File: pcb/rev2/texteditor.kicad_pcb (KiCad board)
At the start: 2 copper layers, 82 x 55 mm, 21 parts, among them J2 LCD IDC, J3 Power In (7v-20v), J4 LED, J5 Contrast Pot, J6 Brightness Pot, J7 SD_Card_Receptacle, Q1 BC547, SW1 Input Type Switch, SW2 Power Switch, U1 L7805

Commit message: switch towurth socket
need to reroute some stuff now
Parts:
- added C5: 100nF, Capacitor_THT:C_Disc_D4.7mm_W2.5mm_P5.00mm, F.Cu at (122.4, 143.6)
- added C6: 10uF, Capacitor_THT:C_Radial_D4.0mm_H5.0mm_P1.50mm, F.Cu at (136.2, 140.2)
- added J1: Unsaved Changes LED, Connector_JST:JST_XA_B02B-XASK-1_1x02_P2.50mm_Vertical, F.Cu at (165.5, 170.2)
- added R3: 220Ω, Resistor_THT:R_Axial_DIN0207_L6.3mm_D2.5mm_P10.16mm_Horizontal, F.Cu at (122.4, 139.5)
- J7: footprint Connector_Card:SD_TE_2041021 -> wurth:693063010911
- moved C4 1.49 mm to (187.5, 99.3)
- moved J7 1.17 mm to (171.5, 116.0)
- moved C3 0.35 mm to (182.8, 99.0)
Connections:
- A1 pad 6: unconnected-(A1-GPIO4-Pad6) -> Net-(A1-GPIO4)
- J4 pad 2: GND -> Net-(J4-Pin_2)
- Q1 pad 1: +5V -> Net-(J4-Pin_2)
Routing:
- net GND: track 49.0 -> 0.00 mm, vias 4 -> 0
- net CD: track 45.3 -> 0.00 mm, vias 1 -> 0
- net /CS: track 43.3 -> 0.00 mm, vias 2 -> 0
- net /TX: track 32.4 -> 0.00 mm
- net /RX: track 30.1 -> 0.00 mm
- net /SCK: track 28.0 -> 0.00 mm
- net +3V3: track 22.1 -> 0.00 mm

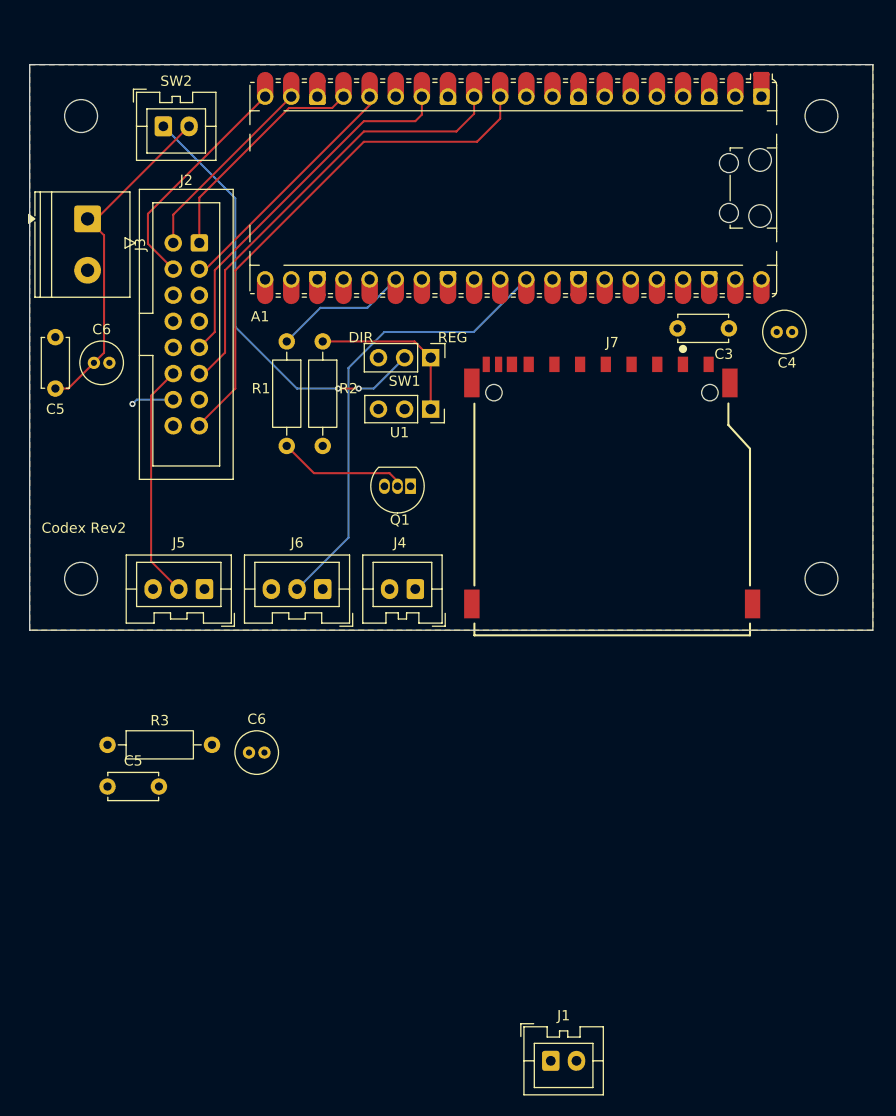
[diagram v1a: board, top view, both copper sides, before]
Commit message: Re-routed new socket footprint
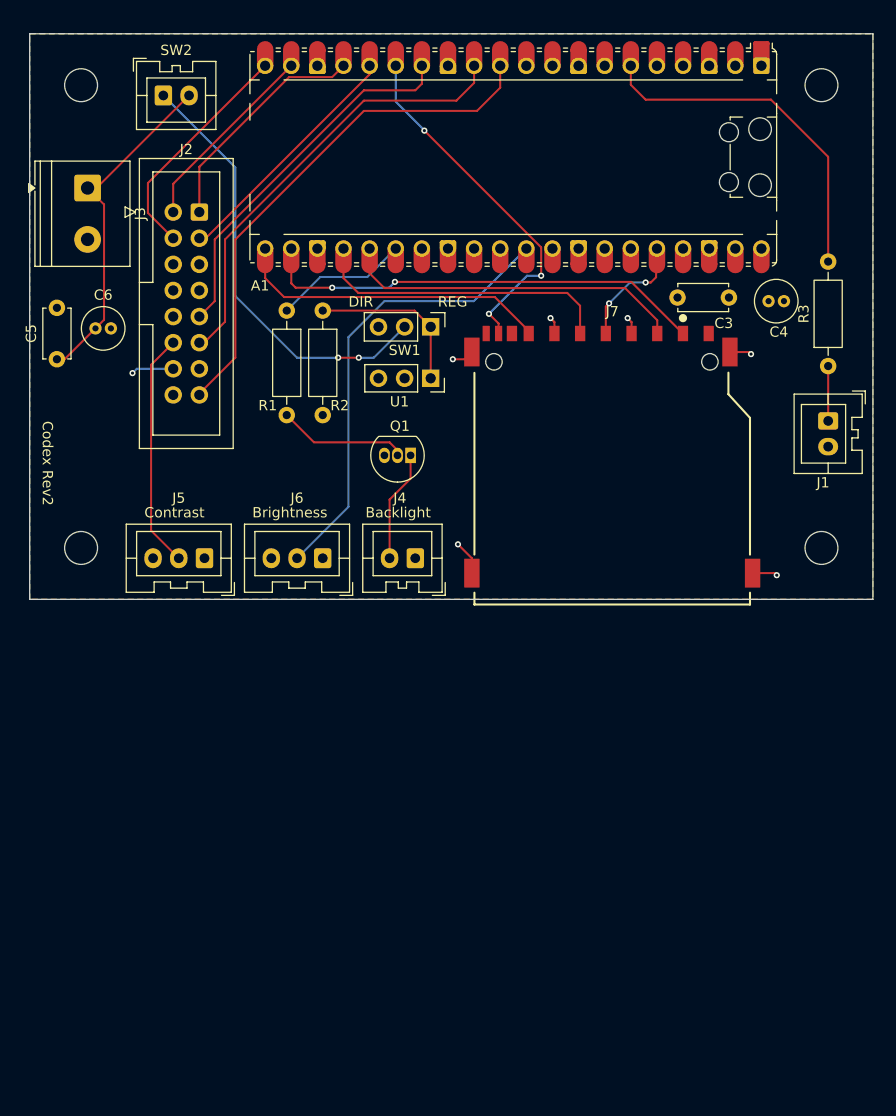
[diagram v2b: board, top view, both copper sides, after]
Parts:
- removed the C5 at (117.3, 104.8)
- removed the C6 at (121.1, 102.3)
- moved R3 79.2 mm to (192.5, 102.7), turned to 90 degrees
- moved J1 67.8 mm to (192.5, 108.0), turned to -90 degrees
- moved C6 43.9 mm to (121.2, 99.0)
- moved C5 41.8 mm to (117.5, 102.0), turned to 90 degrees
- moved C4 3.10 mm to (186.7, 96.3)
- moved A1 3.00 mm to (161.9, 82.3)
- moved C3 3.00 mm to (182.8, 96.0)
- moved J2 3.00 mm to (128.8, 87.7)
- moved J3 3.00 mm to (120.5, 85.3)
- moved J4 3.00 mm to (152.3, 121.3)
- moved J5 3.00 mm to (131.8, 121.3)
- moved J6 3.00 mm to (143.3, 121.3)
- moved J7 3.00 mm to (171.5, 113.0)
- moved Q1 3.00 mm to (151.9, 111.3)
- moved R1 3.00 mm to (139.8, 97.3)
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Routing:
- net /CS: track 0.00 -> 43.2 mm, vias 0 -> 2
- net CD: track 0.00 -> 35.2 mm, vias 0 -> 3
- net Net-(A1-GPIO4): track 0.00 -> 34.1 mm
- net /TX: track 0.00 -> 32.8 mm
- net /RX: track 0.00 -> 30.1 mm
- net /SCK: track 0.00 -> 28.9 mm
- net GND: track 0.00 -> 13.4 mm, vias 0 -> 6
- net Net-(J4-Pin_2): track 0.00 -> 10.8 mm
- net +3V3: track 0.00 -> 10.7 mm, vias 0 -> 2
- net Net-(J1-Pin_1): track 0.00 -> 5.34 mm
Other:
- board text added: "Backlight"
- board text added: "Brightness"
- board text added: "Contrast"

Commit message: add some extra silkscreen to pcb
flip a symbol on the schematic so routing is less dumb
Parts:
- moved SW2 1.85 mm to (127.8, 74.5)
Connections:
- SW2 pad 1: Net-(SW1-B) -> Net-(J3-Pin_1)
- SW2 pad 2: Net-(J3-Pin_1) -> Net-(SW1-B)
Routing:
- net Net-(SW1-B): track 42.6 -> 44.4 mm
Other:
- board text added: "Power Switch"
- board text added: "Unsaved Changes LED"
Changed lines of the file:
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@@
 		(tags "connector JST XA vertical")
 		(property "Reference" "J1"
-			(at 6 0.5 180)
+			(at 2 4.5 180)
 			(layer "F.SilkS")
 			(effects
@@
 	(footprint "Connector_JST:JST_XA_B02B-XASK-1_1x02_P2.50mm_Vertical"
 		(layer "F.Cu")
-		(at 127.85 76.35)
+		(at 127.85 74.5)
 		(descr "JST XA series connector, B02B-XASK-1 (https://www.jst.com/wp-content/uploads/2021/01/eXA1.pdf)")
 		(tags "connector JST XA vertical")
 		(property "Reference" "SW2"
-			(at 1.25 -4.4 0)
+			(at -4.85 -2.5 0)
 			(layer "F.SilkS")
 			(effects
@@
 			(remove_unused_layers no)
 			(roundrect_rratio 0.147059)
-			(net "Net-(SW1-B)")
+			(net "Net-(J3-Pin_1)")
 			(pinfunction "A_1")
 			(pintype "passive")
@@
 			(layers "*.Cu" "*.Mask")
 			(remove_unused_layers no)
-			(net "Net-(J3-Pin_1)")
+			(net "Net-(SW1-B)")
 			(pinfunction "B_2")
 			(pintype "passive")
@@
 		(layer "Edge.Cuts")
 	)
+	(gr_text "Power Switch"
+		(at 124 79.5 0)
+		(layer "F.SilkS")
+		(effects
+			(font
+				(size 1 1)
+				(thickness 0.1)
+			)
+			(justify left bottom)
+		)
+	)
 	(gr_text "Contrast"
 		(at 126 117.5 0)
@@
 		)
 	)
+	(gr_text "Unsaved \nChanges LED"
+		(at 191.5 116.5 0)
+		(layer "F.SilkS")
+		(effects
+			(font
+				(size 1 1)
+				(thickness 0.1)
+			)
+			(justify bottom)
+		)
+	)
 	(gr_text "Codex Rev2"
 		(at 116 108 270)
@@
 	)
 	(segment
-		(start 140.85 101.85)
-		(end 144.85 101.85)
+		(start 134.85 95.85)
+		(end 140.85 101.85)
 		(width 0.2)
 		(layer "B.Cu")
@@
 	)
 	(segment
-		(start 134.85 95.85)
-		(end 140.85 101.85)
+		(start 148.31 101.85)
+		(end 151.31 98.85)
 		(width 0.2)
 		(layer "B.Cu")
@@
 	)
 	(segment
-		(start 134.85 83.35)
+		(start 134.85 77.35)
 		(end 134.85 95.85)
 		(width 0.2)
@@
 	)
 	(segment
-		(start 148.31 101.85)
-		(end 151.31 98.85)
+		(start 146.85 101.85)
+		(end 148.31 101.85)
 		(width 0.2)
 		(layer "B.Cu")
@@
 	)
 	(segment
-		(start 127.85 76.35)
-		(end 134.85 83.35)
+		(start 140.85 101.85)
+		(end 144.85 101.85)
 		(width 0.2)
 		(layer "B.Cu")
@@
 	)
 	(segment
-		(start 146.85 101.85)
-		(end 148.31 101.85)
+		(start 130.35 74.5)
+		(end 132 74.5)
+		(width 0.2)
+		(layer "B.Cu")
+		(net "Net-(SW1-B)")
+	)
+	(segment
+		(start 132 74.5)
+		(end 134.85 77.35)
 		(width 0.2)
 		(layer "B.Cu")
@@
 	)
 	(segment
-		(start 121.35 85.35)
-		(end 130.35 76.35)
+		(start 121.25 99)
+		(end 118.25 102)
 		(width 0.2)
 		(layer "F.Cu")
@@
 	)
 	(segment
-		(start 121.25 99)
-		(end 118.25 102)
+		(start 122.0825 98.1675)
+		(end 122.0825 86.95)
 		(width 0.2)
 		(layer "F.Cu")
@@
 	)
 	(segment
-		(start 120.4825 85.35)
-		(end 121.35 85.35)
+		(start 120.4825 81.8675)
+		(end 127.85 74.5)
 		(width 0.2)
 		(layer "F.Cu")
@@
 	)
 	(segment
-		(start 122.0825 98.1675)
-		(end 122.0825 86.95)
+		(start 120.4825 85.35)
+		(end 120.4825 81.8675)
 		(width 0.2)
 		(layer "F.Cu")

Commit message: Some board and schematic adjustments
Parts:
- removed SW2: Power Switch, Connector_JST:JST_XA_B02B-XASK-1_1x02_P2.50mm_Vertical
- added J8: To Power Switch, Connector_JST:JST_XA_B02B-XASK-1_1x02_P2.50mm_Vertical, F.Cu at (127.8, 74.5)
- J1: value Unsaved Changes LED -> To Unsaved Changes LED
- J4: value LED -> To LED Backlight
- J6: value Brightness Pot -> To Brightness Pot
- SW1: footprint Connector_PinHeader_2.54mm:PinHeader_1x03_P2.54mm_Vertical -> SLW_883935_2A_D:SW_SLW-883935-2A-D
- U1: footprint Connector_PinSocket_2.54mm:PinSocket_1x03_P2.54mm_Vertical -> Package_TO_SOT_THT:TO-220-3_Vertical
- moved SW1 2.60 mm to (151.2, 98.8), turned to 180 degrees
- moved U1 0.10 mm to (153.8, 103.8), turned to 180 degrees
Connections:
- net /BRI renamed /BRIGHTNESS
- net CD renamed /CD
- net D4 renamed /D4
- net D5 renamed /D5
- net D6 renamed /D6
- net D7 renamed /D7
- net E1 renamed /E1
- net E2 renamed /E2
- net Net-(A1-GPIO4) renamed /UNSAVED_LED
- net Net-(J3-Pin_1) renamed VIN
- net RS renamed /RS

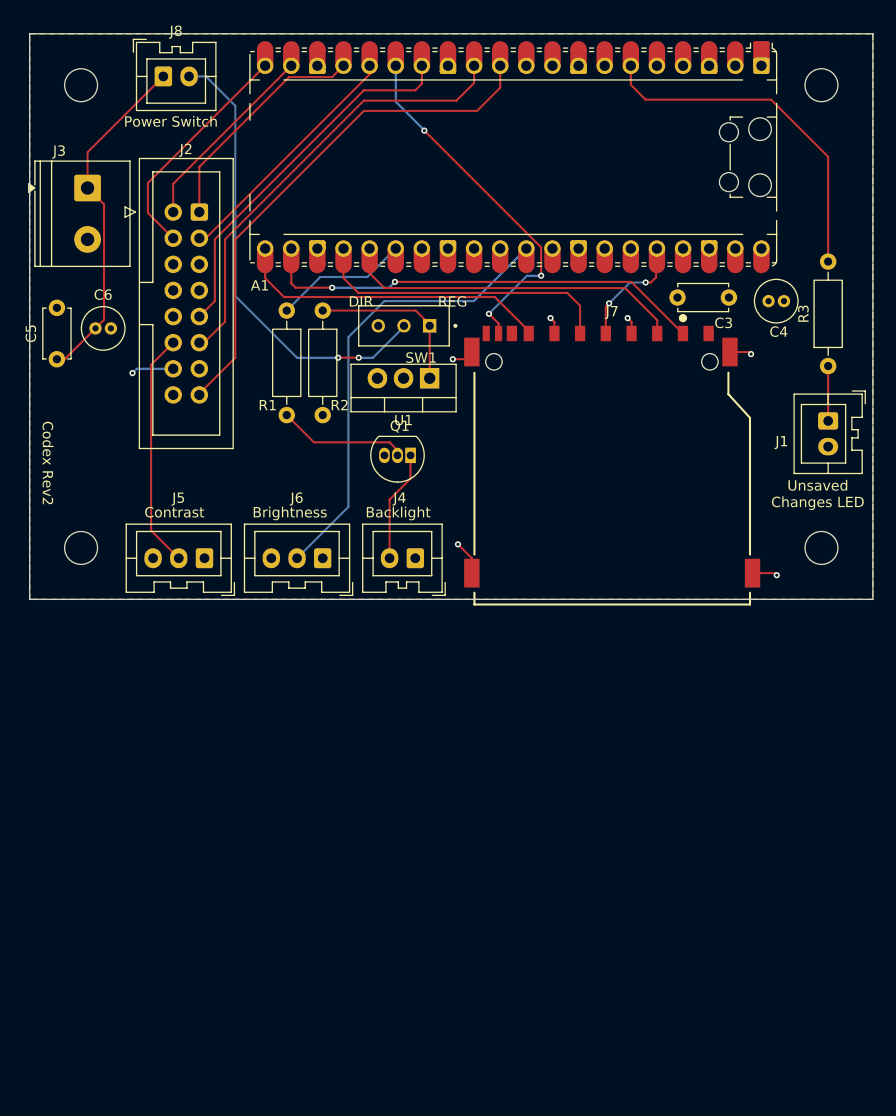
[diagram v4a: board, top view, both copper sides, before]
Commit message: Small pcb tweaks
moved around some silkscreens, widened vias and power traces
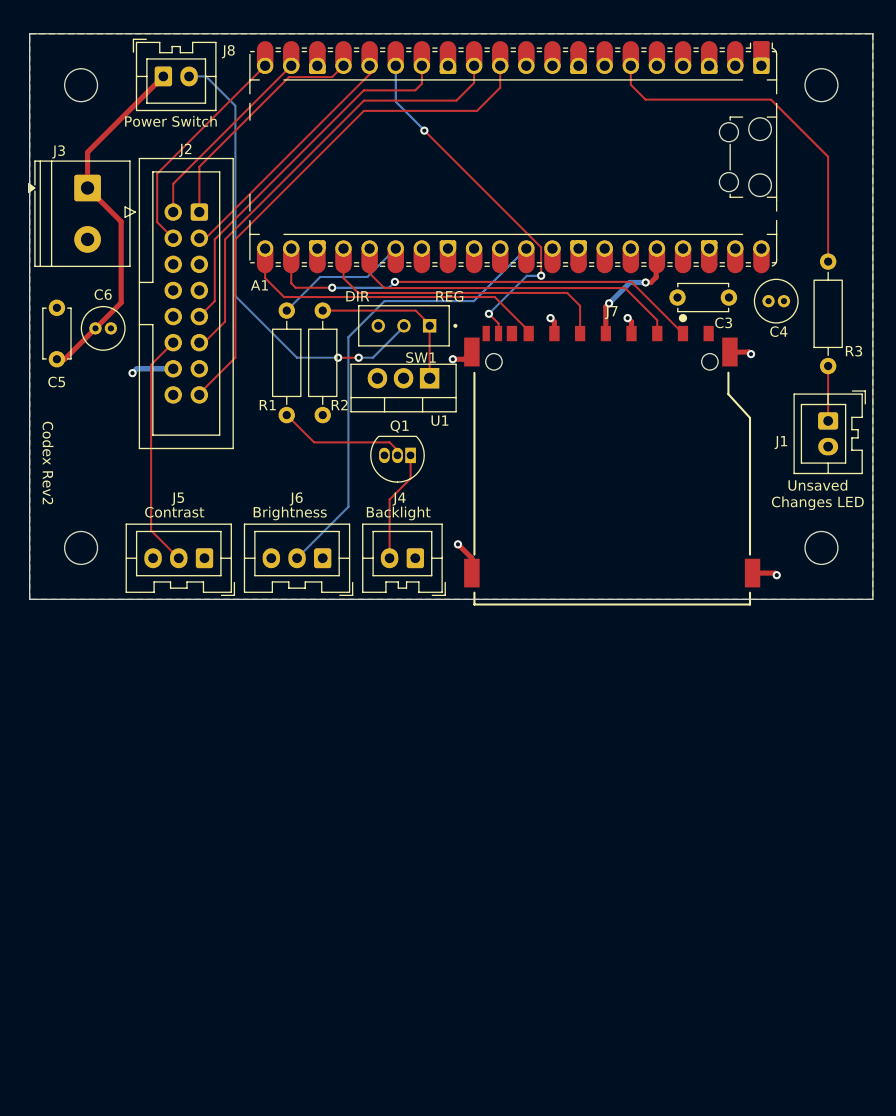
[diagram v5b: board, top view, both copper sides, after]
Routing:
- net VIN: track 33.6 -> 34.9 mm
- net /D4: track 22.5 -> 21.8 mm
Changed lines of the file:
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@@
 		(tags "TO-220-3 Vertical RM 2.54mm")
 		(property "Reference" "U1"
-			(at 2.54 -4.1 0)
+			(at -1 -4.15 0)
 			(layer "F.SilkS")
 			(effects
@@
 		(tags "Resistor Axial_DIN0207 series Axial Horizontal pin pitch 10.16mm 0.25W = 1/4W length 6.3mm diameter 2.5mm")
 		(property "Reference" "R3"
-			(at 5.08 -2.37 90)
+			(at 1.414 2.5 180)
 			(layer "F.SilkS")
 			(effects
@@
 		(tags "C Disc series Radial pin pitch 5.00mm diameter 4.7mm width 2.5mm Capacitor")
 		(property "Reference" "C5"
-			(at 2.5 -2.5 90)
+			(at -2.25 0 0)
 			(layer "F.SilkS")
 			(effects
@@
 		(tags "connector JST XA vertical")
 		(property "Reference" "J8"
-			(at 1.25 -4.4 0)
+			(at 6.4 -2.5 0)
 			(layer "F.SilkS")
 			(effects
@@
 	)
 	(gr_text "DIR"
-		(at 145.85 97 0)
+		(at 145.5 96.5 0)
 		(layer "F.SilkS")
 		(effects
@@
 	)
 	(gr_text "REG"
-		(at 154.54 97 0)
+		(at 154.25 96.5 0)
 		(layer "F.SilkS")
 		(effects
@@
 	(via
 		(at 144.85 101.85)
-		(size 0.6)
-		(drill 0.3)
+		(size 0.8)
+		(drill 0.4)
 		(layers "F.Cu" "B.Cu")
 		(net "Net-(J8-Pin_2)")
@@
 	(via
 		(at 146.85 101.85)
-		(size 0.6)
-		(drill 0.3)
+		(size 0.8)
+		(drill 0.4)
 		(layers "F.Cu" "B.Cu")
 		(net "Net-(J8-Pin_2)")
@@
 	(via
 		(at 124.85 103.35)
-		(size 0.6)
-		(drill 0.3)
+		(size 0.8)
+		(drill 0.4)
 		(layers "F.Cu" "B.Cu")
 		(net "+5V")
@@
 		(start 125.27 102.93)
 		(end 124.85 103.35)
-		(width 0.2)
+		(width 0.5)
 		(layer "B.Cu")
 		(net "+5V")
@@
 		(start 128.81 102.93)
 		(end 125.27 102.93)
-		(width 0.2)
+		(width 0.5)
 		(layer "B.Cu")
 		(net "+5V")
@@
 		(start 165.88 98.38)
 		(end 165.5 98)
-		(width 0.2)
+		(width 0.5)
 		(layer "F.Cu")
 		(net "GND")
@@
 		(start 157.85 121.35)
 		(end 156.5 120)
-		(width 0.2)
+		(width 0.5)
 		(layer "F.Cu")
 		(net "GND")
@@
 		(start 165.88 99.5)
 		(end 165.88 98.38)
-		(width 0.2)
+		(width 0.5)
 		(layer "F.Cu")
 		(net "GND")
@@
 		(start 157.15 102)
 		(end 157.85 101.3)
-		(width 0.2)
+		(width 0.5)
 		(layer "F.Cu")
 		(net "GND")
@@
 		(start 173.38 98.38)
 		(end 173 98)
-		(width 0.2)
+		(width 0.5)
 		(layer "F.Cu")
 		(net "GND")
@@
 		(start 185.15 122.8)
 		(end 187.3 122.8)
-		(width 0.2)
+		(width 0.5)
 		(layer "F.Cu")
 		(net "GND")
@@
 		(start 173.38 99.5)
 		(end 173.38 98.38)
-		(width 0.2)
+		(width 0.5)
 		(layer "F.Cu")
 		(net "GND")
@@
 		(start 156 102)
 		(end 157.15 102)
-		(width 0.2)
+		(width 0.5)
 		(layer "F.Cu")
 		(net "GND")
@@
 		(start 187.3 122.8)
 		(end 187.5 123)
-		(width 0.2)
+		(width 0.5)
 		(layer "F.Cu")
 		(net "GND")
@@
 		(start 184.8 101.3)
 		(end 185 101.5)
-		(width 0.2)
+		(width 0.5)
 		(layer "F.Cu")
 		(net "GND")
@@
 		(start 182.95 101.3)
 		(end 184.8 101.3)
-		(width 0.2)
+		(width 0.5)
 		(layer "F.Cu")
 		(net "GND")
@@
 		(start 157.85 122.8)
 		(end 157.85 121.35)
-		(width 0.2)
+		(width 0.5)
 		(layer "F.Cu")
 		(net "GND")
@@
 	(via
 		(at 187.5 123)
-		(size 0.6)
-		(drill 0.3)
+		(size 0.8)
+		(drill 0.4)
 		(layers "F.Cu" "B.Cu")
 		(net "GND")
@@
 	(via
 		(at 185 101.5)
-		(size 0.6)
-		(drill 0.3)
+		(size 0.8)
+		(drill 0.4)
 		(layers "F.Cu" "B.Cu")
 		(net "GND")
@@
 	(via
 		(at 173 98)
-		(size 0.6)
-		(drill 0.3)
+		(size 0.8)
+		(drill 0.4)
 		(layers "F.Cu" "B.Cu")
 		(net "GND")
@@
 	(via
 		(at 165.5 98)
-		(size 0.6)
-		(drill 0.3)
+		(size 0.8)
+		(drill 0.4)
 		(layers "F.Cu" "B.Cu")
 		(net "GND")
@@
 	(via
 		(at 156 102)
-		(size 0.6)
-		(drill 0.3)
+		(size 0.8)
+		(drill 0.4)
 		(layers "F.Cu" "B.Cu")
 		(net "GND")
@@
 	(via
 		(at 156.5 120)
-		(size 0.6)
-		(drill 0.3)
+		(size 0.8)
+		(drill 0.4)
 		(layers "F.Cu" "B.Cu")
 		(net "GND")
@@
 	)
 	(segment
-		(start 126.35 84.86)
-		(end 137.75 73.46)
+		(start 128.81 90.23)
+		(end 127.25 88.67)
 		(width 0.2)
 		(layer "F.Cu")
@@
 	)
 	(segment
-		(start 126.35 87.77)
-		(end 126.35 84.86)
+		(start 127.25 83.96)
+		(end 137.75 73.46)
 		(width 0.2)
 		(layer "F.Cu")
@@
 	)
 	(segment
-		(start 128.81 90.23)
-		(end 126.35 87.77)
+		(start 127.25 88.67)
+		(end 127.25 83.96)
 		(width 0.2)
 		(layer "F.Cu")
@@
 	(via
 		(at 144.272 95.044)
-		(size 0.6)
-		(drill 0.3)
+		(size 0.8)
+		(drill 0.4)
 		(layers "F.Cu" "B.Cu")
 		(net "/CS")
@@
 	(via
 		(at 150.368 94.477746)
-		(size 0.6)
-		(drill 0.3)
+		(size 0.8)
+		(drill 0.4)
 		(layers "F.Cu" "B.Cu")
 		(net "/CS")
@@
 		(start 170.88 99.5)
 		(end 170.88 96.884)
-		(width 0.2)
+		(width 0.5)
 		(layer "F.Cu")
 		(net "+3V3")
@@
 		(start 175.768 92.122)
 		(end 175.85 92.04)
-		(width 0.2)
+		(width 0.5)
 		(layer "F.Cu")
 		(net "+3V3")
@@
 		(start 175.26 94.536)
 		(end 175.768 94.028)
-		(width 0.2)
+		(width 0.5)
 		(layer "F.Cu")
 		(net "+3V3")
@@
 		(start 174.752 94.536)
 		(end 175.26 94.536)
-		(width 0.2)
+		(width 0.5)
 		(layer "F.Cu")
 		(net "+3V3")
@@
 		(start 170.88 96.884)
 		(end 171.196 96.568)
-		(width 0.2)
+		(width 0.5)
 		(layer "F.Cu")
 		(net "+3V3")
@@
 		(start 175.768 94.028)
 		(end 175.768 92.122)
-		(width 0.2)
+		(width 0.5)
 		(layer "F.Cu")
 		(net "+3V3")
@@
 	(via
 		(at 171.196 96.568)
-		(size 0.6)
-		(drill 0.3)
+		(size 0.8)
+		(drill 0.4)
 		(layers "F.Cu" "B.Cu")
 		(net "+3V3")
@@
 	(via
 		(at 174.752 94.536)
-		(size 0.6)
-		(drill 0.3)
+		(size 0.8)
+		(drill 0.4)
 		(layers "F.Cu" "B.Cu")
 		(net "+3V3")
@@
 		(start 173.228 94.536)
 		(end 174.752 94.536)
-		(width 0.2)
+		(width 0.5)
 		(layer "B.Cu")
 		(net "+3V3")
@@
 		(start 171.196 96.568)
 		(end 173.228 94.536)
-		(width 0.2)
+		(width 0.5)
 		(layer "B.Cu")
 		(net "+3V3")
@@
 	(via
 		(at 164.592 93.877746)
-		(size 0.6)
-		(drill 0.3)
+		(size 0.8)
+		(drill 0.4)
 		(layers "F.Cu" "B.Cu")
 		(net "/CD")
@@
 	(via
 		(at 153.232818 79.767182)
-		(size 0.6)
-		(drill 0.3)
+		(size 0.8)
+		(drill 0.4)
 		(layers "F.Cu" "B.Cu")
 		(net "/CD")
@@
 	(via
 		(at 159.512 97.584)
-		(size 0.6)
-		(drill 0.3)
+		(size 0.8)
+		(drill 0.4)
 		(layers "F.Cu" "B.Cu")
 		(net "/CD")
@@
 	)
 	(segment
-		(start 122.0825 86.95)
-		(end 120.4825 85.35)
-		(width 0.2)
+		(start 121.25 99)
+		(end 123.75 96.5)
+		(width 0.5)
 		(layer "F.Cu")
 		(net "VIN")
@@
 		(start 121.25 99)
 		(end 118.25 102)
-		(width 0.2)
+		(width 0.5)
 		(layer "F.Cu")
 		(net "VIN")
 	)
 	(segment
-		(start 122.0825 98.1675)
-		(end 122.0825 86.95)
-		(width 0.2)
+		(start 123.75 88.6175)
+		(end 120.4825 85.35)
+		(width 0.5)
 		(layer "F.Cu")
 		(net "VIN")
@@
 		(start 120.4825 81.8675)
 		(end 127.85 74.5)
-		(width 0.2)
+		(width 0.5)
 		(layer "F.Cu")
 		(net "VIN")
 	)
 	(segment
-		(start 120.4825 85.35)
-		(end 120.4825 81.8675)
-		(width 0.2)
+		(start 123.75 96.5)
+		(end 123.75 88.6175)
+		(width 0.5)
 		(layer "F.Cu")
 		(net "VIN")
 	)
 	(segment
-		(start 118.25 102)
-		(end 117.5 102)
-		(width 0.2)
+		(start 120.4825 85.35)
+		(end 120.4825 81.8675)
+		(width 0.5)
 		(layer "F.Cu")
 		(net "VIN")
 	)
 	(segment
-		(start 121.25 99)
-		(end 122.0825 98.1675)
-		(width 0.2)
+		(start 118.25 102)
+		(end 117.5 102)
+		(width 0.5)
 		(layer "F.Cu")
 		(net "VIN")
